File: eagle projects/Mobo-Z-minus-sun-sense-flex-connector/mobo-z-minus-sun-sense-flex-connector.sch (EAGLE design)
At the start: 2 parts

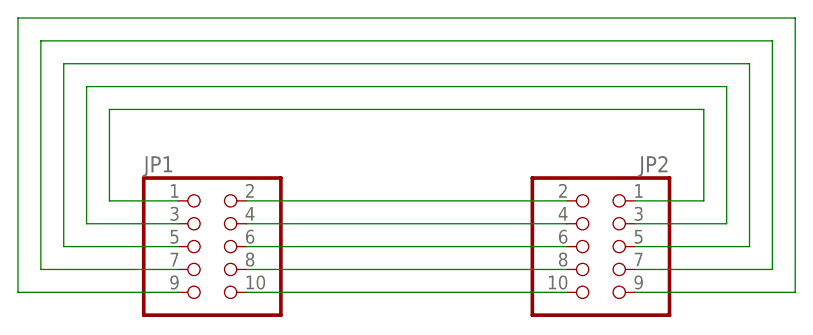
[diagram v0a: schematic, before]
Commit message: Created 5x2 SMD 2.54mm footprint and added it to board that needs it
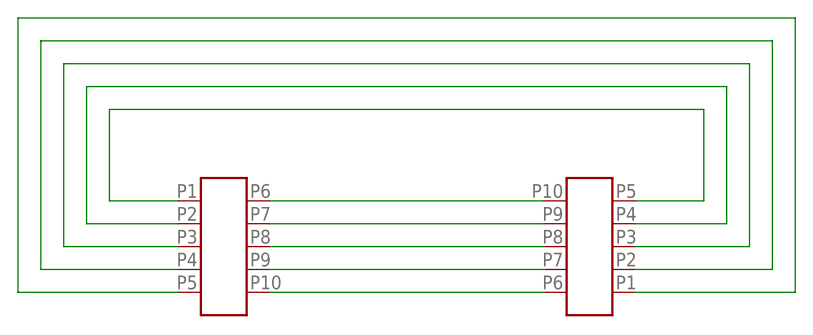
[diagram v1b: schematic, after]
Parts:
- removed JP1, JP2: (no value), pinhead:PINHD-2X5
- added X1, X2: 5X2_SMD_2.54MM_HEADER, SMD_headers:5X2_SMD_2.54MM_HEADER
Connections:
- net N$1: now also X1.P6, X2.P10; no longer JP1.2, JP2.2
- net N$10: now also X1.P5, X2.P1; no longer JP1.9, JP2.9
- net N$2: now also X1.P7, X2.P9; no longer JP1.4, JP2.4
- net N$3: now also X1.P8, X2.P8; no longer JP1.6, JP2.6
- net N$4: now also X1.P9, X2.P7; no longer JP1.8, JP2.8
- net N$5: now also X1.P10, X2.P6; no longer JP1.10, JP2.10
- net N$6: now also X1.P1, X2.P5; no longer JP1.1, JP2.1
- net N$7: now also X1.P2\, X2.P4; no longer JP1.3, JP2.3
- net N$8: now also X1.P3, X2.P3; no longer JP1.5, JP2.5
- net N$9: now also X1.P4, X2.P2\; no longer JP1.7, JP2.7
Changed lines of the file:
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@@
 </classes>
 <parts>
-<part name="JP1" library="pinhead" library_urn="urn:adsk.eagle:library:325" deviceset="PINHD-2X5" device="" package3d_urn="urn:adsk.eagle:package:22470/2"/>
-<part name="JP2" library="pinhead" library_urn="urn:adsk.eagle:library:325" deviceset="PINHD-2X5" device="" package3d_urn="urn:adsk.eagle:package:22470/2"/>
+<part name="X1" library="SMD_headers" deviceset="5X2_SMD_2.54MM_HEADER" device=""/>
+<part name="X2" library="SMD_headers" deviceset="5X2_SMD_2.54MM_HEADER" device=""/>
 </parts>
 <sheets>
@@
 </plain>
 <instances>
-<instance part="JP1" gate="A" x="30.48" y="53.34" smashed="yes">
-<attribute name="NAME" x="24.13" y="61.595" size="1.778" layer="95"/>
-<attribute name="VALUE" x="24.13" y="43.18" size="1.778" layer="96"/>
-</instance>
-<instance part="JP2" gate="A" x="76.2" y="53.34" smashed="yes" rot="MR0">
-<attribute name="NAME" x="82.55" y="61.595" size="1.778" layer="95" rot="MR0"/>
-<attribute name="VALUE" x="82.55" y="43.18" size="1.778" layer="96" rot="MR0"/>
-</instance>
+<instance part="X1" gate="G$1" x="33.02" y="53.34" smashed="yes"/>
+<instance part="X2" gate="G$1" x="73.66" y="53.34" smashed="yes" rot="R180"/>
 </instances>
 <busses>
 </busses>
 <nets>
+<net name="N$6" class="0">
+<segment>
+<wire x1="27.94" y1="58.42" x2="20.32" y2="58.42" width="0.1524" layer="91"/>
+<wire x1="20.32" y1="58.42" x2="20.32" y2="68.58" width="0.1524" layer="91"/>
+<wire x1="20.32" y1="68.58" x2="86.36" y2="68.58" width="0.1524" layer="91"/>
+<wire x1="86.36" y1="68.58" x2="86.36" y2="58.42" width="0.1524" layer="91"/>
+<wire x1="86.36" y1="58.42" x2="78.74" y2="58.42" width="0.1524" layer="91"/>
+<pinref part="X1" gate="G$1" pin="P1"/>
+<pinref part="X2" gate="G$1" pin="P5"/>
+</segment>
+</net>
+<net name="N$7" class="0">
+<segment>
+<wire x1="27.94" y1="55.88" x2="17.78" y2="55.88" width="0.1524" layer="91"/>
+<wire x1="17.78" y1="55.88" x2="17.78" y2="71.12" width="0.1524" layer="91"/>
+<wire x1="17.78" y1="71.12" x2="88.9" y2="71.12" width="0.1524" layer="91"/>
+<wire x1="88.9" y1="71.12" x2="88.9" y2="55.88" width="0.1524" layer="91"/>
+<wire x1="88.9" y1="55.88" x2="78.74" y2="55.88" width="0.1524" layer="91"/>
+<pinref part="X1" gate="G$1" pin="P2\"/>
+<pinref part="X2" gate="G$1" pin="P4"/>
+</segment>
+</net>
+<net name="N$8" class="0">
+<segment>
+<wire x1="78.74" y1="53.34" x2="91.44" y2="53.34" width="0.1524" layer="91"/>
+<wire x1="91.44" y1="53.34" x2="91.44" y2="73.66" width="0.1524" layer="91"/>
+<wire x1="91.44" y1="73.66" x2="15.24" y2="73.66" width="0.1524" layer="91"/>
+<wire x1="15.24" y1="73.66" x2="15.24" y2="53.34" width="0.1524" layer="91"/>
+<wire x1="15.24" y1="53.34" x2="27.94" y2="53.34" width="0.1524" layer="91"/>
+<pinref part="X1" gate="G$1" pin="P3"/>
+<pinref part="X2" gate="G$1" pin="P3"/>
+</segment>
+</net>
+<net name="N$9" class="0">
+<segment>
+<wire x1="27.94" y1="50.8" x2="12.7" y2="50.8" width="0.1524" layer="91"/>
+<wire x1="12.7" y1="50.8" x2="12.7" y2="76.2" width="0.1524" layer="91"/>
+<wire x1="12.7" y1="76.2" x2="93.98" y2="76.2" width="0.1524" layer="91"/>
+<wire x1="93.98" y1="76.2" x2="93.98" y2="50.8" width="0.1524" layer="91"/>
+<wire x1="93.98" y1="50.8" x2="78.74" y2="50.8" width="0.1524" layer="91"/>
+<pinref part="X1" gate="G$1" pin="P4"/>
+<pinref part="X2" gate="G$1" pin="P2\"/>
+</segment>
+</net>
+<net name="N$10" class="0">
+<segment>
+<wire x1="27.94" y1="48.26" x2="10.16" y2="48.26" width="0.1524" layer="91"/>
+<wire x1="10.16" y1="48.26" x2="10.16" y2="78.74" width="0.1524" layer="91"/>
+<wire x1="10.16" y1="78.74" x2="96.52" y2="78.74" width="0.1524" layer="91"/>
+<wire x1="96.52" y1="78.74" x2="96.52" y2="48.26" width="0.1524" layer="91"/>
+<wire x1="96.52" y1="48.26" x2="78.74" y2="48.26" width="0.1524" layer="91"/>
+<pinref part="X1" gate="G$1" pin="P5"/>
+<pinref part="X2" gate="G$1" pin="P1"/>
+</segment>
+</net>
 <net name="N$1" class="0">
 <segment>
-<pinref part="JP1" gate="A" pin="2"/>
-<pinref part="JP2" gate="A" pin="2"/>
-<wire x1="35.56" y1="58.42" x2="71.12" y2="58.42" width="0.1524" layer="91"/>
+<pinref part="X1" gate="G$1" pin="P6"/>
+<wire x1="38.1" y1="58.42" x2="68.58" y2="58.42" width="0.1524" layer="91"/>
+<pinref part="X2" gate="G$1" pin="P10"/>
 </segment>
 </net>
 <net name="N$2" class="0">
 <segment>
-<pinref part="JP1" gate="A" pin="4"/>
-<pinref part="JP2" gate="A" pin="4"/>
-<wire x1="35.56" y1="55.88" x2="71.12" y2="55.88" width="0.1524" layer="91"/>
+<pinref part="X1" gate="G$1" pin="P7"/>
+<wire x1="38.1" y1="55.88" x2="68.58" y2="55.88" width="0.1524" layer="91"/>
+<pinref part="X2" gate="G$1" pin="P9"/>
 </segment>
 </net>
 <net name="N$3" class="0">
 <segment>
-<pinref part="JP1" gate="A" pin="6"/>
-<pinref part="JP2" gate="A" pin="6"/>
-<wire x1="35.56" y1="53.34" x2="71.12" y2="53.34" width="0.1524" layer="91"/>
+<pinref part="X1" gate="G$1" pin="P8"/>
+<wire x1="38.1" y1="53.34" x2="68.58" y2="53.34" width="0.1524" layer="91"/>
+<pinref part="X2" gate="G$1" pin="P8"/>
 </segment>
 </net>
 <net name="N$4" class="0">
 <segment>
-<pinref part="JP1" gate="A" pin="8"/>
-<pinref part="JP2" gate="A" pin="8"/>
-<wire x1="35.56" y1="50.8" x2="71.12" y2="50.8" width="0.1524" layer="91"/>
+<pinref part="X1" gate="G$1" pin="P9"/>
+<wire x1="38.1" y1="50.8" x2="68.58" y2="50.8" width="0.1524" layer="91"/>
+<pinref part="X2" gate="G$1" pin="P7"/>
 </segment>
 </net>
 <net name="N$5" class="0">
 <segment>
-<pinref part="JP1" gate="A" pin="10"/>
-<pinref part="JP2" gate="A" pin="10"/>
-<wire x1="35.56" y1="48.26" x2="71.12" y2="48.26" width="0.1524" layer="91"/>
-</segment>
-</net>
-<net name="N$6" class="0">
-<segment>
-<pinref part="JP1" gate="A" pin="1"/>
-<wire x1="27.94" y1="58.42" x2="20.32" y2="58.42" width="0.1524" layer="91"/>
-<wire x1="20.32" y1="58.42" x2="20.32" y2="68.58" width="0.1524" layer="91"/>
-<wire x1="20.32" y1="68.58" x2="86.36" y2="68.58" width="0.1524" layer="91"/>
-<pinref part="JP2" gate="A" pin="1"/>
-<wire x1="86.36" y1="68.58" x2="86.36" y2="58.42" width="0.1524" layer="91"/>
-<wire x1="86.36" y1="58.42" x2="78.74" y2="58.42" width="0.1524" layer="91"/>
-</segment>
-</net>
-<net name="N$7" class="0">
-<segment>
-<pinref part="JP1" gate="A" pin="3"/>
-<wire x1="27.94" y1="55.88" x2="17.78" y2="55.88" width="0.1524" layer="91"/>
-<wire x1="17.78" y1="55.88" x2="17.78" y2="71.12" width="0.1524" layer="91"/>
-<wire x1="17.78" y1="71.12" x2="88.9" y2="71.12" width="0.1524" layer="91"/>
-<wire x1="88.9" y1="71.12" x2="88.9" y2="55.88" width="0.1524" layer="91"/>
-<pinref part="JP2" gate="A" pin="3"/>
-<wire x1="88.9" y1="55.88" x2="78.74" y2="55.88" width="0.1524" layer="91"/>
-</segment>
-</net>
-<net name="N$8" class="0">
-<segment>
-<pinref part="JP2" gate="A" pin="5"/>
-<wire x1="78.74" y1="53.34" x2="91.44" y2="53.34" width="0.1524" layer="91"/>
-<wire x1="91.44" y1="53.34" x2="91.44" y2="73.66" width="0.1524" layer="91"/>
-<wire x1="91.44" y1="73.66" x2="15.24" y2="73.66" width="0.1524" layer="91"/>
-<wire x1="15.24" y1="73.66" x2="15.24" y2="53.34" width="0.1524" layer="91"/>
-<pinref part="JP1" gate="A" pin="5"/>
-<wire x1="15.24" y1="53.34" x2="27.94" y2="53.34" width="0.1524" layer="91"/>
-</segment>
-</net>
-<net name="N$9" class="0">
-<segment>
-<pinref part="JP1" gate="A" pin="7"/>
-<wire x1="27.94" y1="50.8" x2="12.7" y2="50.8" width="0.1524" layer="91"/>
-<wire x1="12.7" y1="50.8" x2="12.7" y2="76.2" width="0.1524" layer="91"/>
-<wire x1="12.7" y1="76.2" x2="93.98" y2="76.2" width="0.1524" layer="91"/>
-<pinref part="JP2" gate="A" pin="7"/>
-<wire x1="93.98" y1="76.2" x2="93.98" y2="50.8" width="0.1524" layer="91"/>
-<wire x1="93.98" y1="50.8" x2="78.74" y2="50.8" width="0.1524" layer="91"/>
-</segment>
-</net>
-<net name="N$10" class="0">
-<segment>
-<pinref part="JP1" gate="A" pin="9"/>
-<wire x1="27.94" y1="48.26" x2="10.16" y2="48.26" width="0.1524" layer="91"/>
-<wire x1="10.16" y1="48.26" x2="10.16" y2="78.74" width="0.1524" layer="91"/>
-<wire x1="10.16" y1="78.74" x2="96.52" y2="78.74" width="0.1524" layer="91"/>
-<wire x1="96.52" y1="78.74" x2="96.52" y2="48.26" width="0.1524" layer="91"/>
-<pinref part="JP2" gate="A" pin="9"/>
-<wire x1="96.52" y1="48.26" x2="78.74" y2="48.26" width="0.1524" layer="91"/>
+<pinref part="X1" gate="G$1" pin="P10"/>
+<wire x1="38.1" y1="48.26" x2="68.58" y2="48.26" width="0.1524" layer="91"/>
+<pinref part="X2" gate="G$1" pin="P6"/>
 </segment>
 </net>
@@
 </schematic>
 </drawing>
-<compatibility>
-<note version="8.2" severity="warning">
-Since Version 8.2, EAGLE supports online libraries. The ids
-of those online libraries will not be understood (or retained)
-with this version.
-</note>
-<note version="8.3" severity="warning">
-Since Version 8.3, EAGLE supports URNs for individual library
-assets (packages, symbols, and devices). The URNs of those assets
-will not be understood (or retained) with this version.
-</note>
-<note version="8.3" severity="warning">
-Since Version 8.3, EAGLE supports the association of 3D packages
-with devices in libraries, schematics, and board files. Those 3D
-packages will not be understood (or retained) with this version.
-</note>
-</compatibility>
 </eagle>

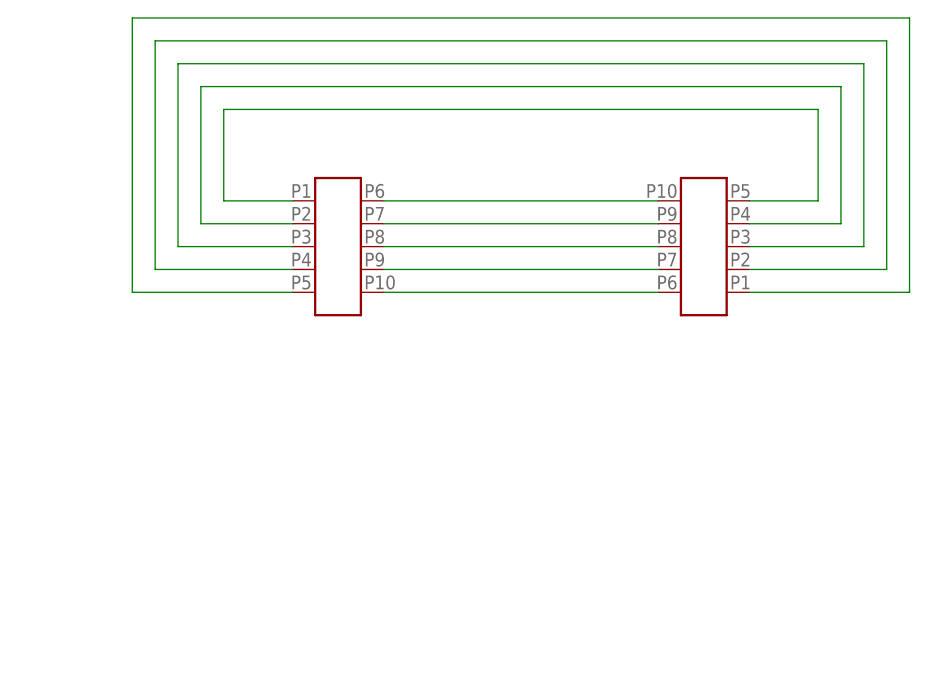
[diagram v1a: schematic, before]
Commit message: Fixed Connector Boards
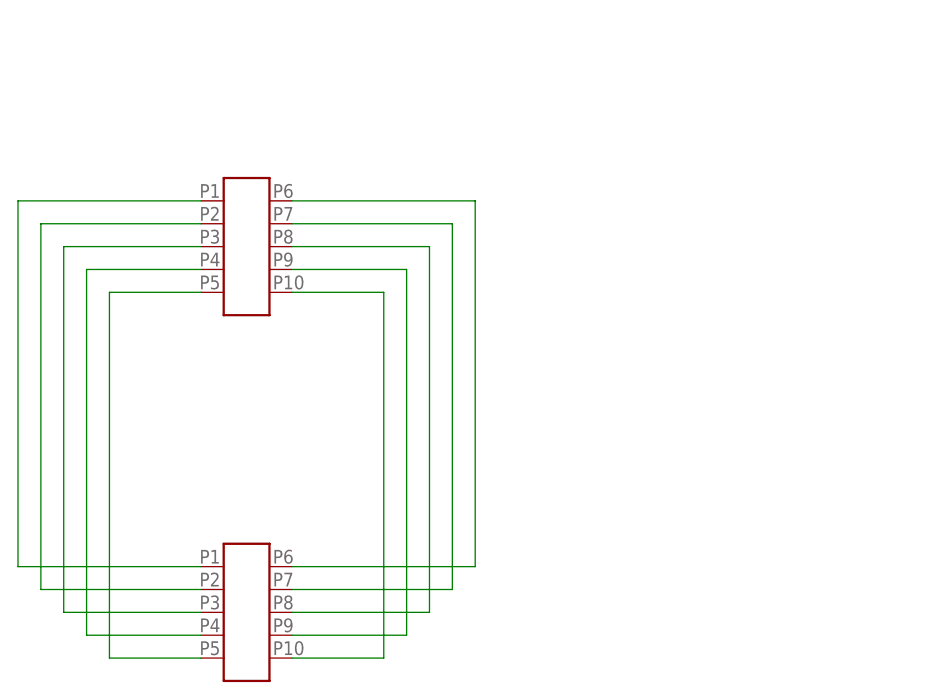
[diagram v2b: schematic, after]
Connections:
- net N$1: now also X2.P6; no longer X2.P10
- net N$10: now also X1.P1; no longer X1.P5
- net N$2: now also X2.P7; no longer X2.P9
- net N$4: now also X2.P9; no longer X2.P7
- net N$5: now also X2.P10; no longer X2.P6
- net N$6: now also X1.P5; no longer X1.P1
- net N$7: now also X1.P4; no longer X1.P2\
- net N$9: now also X1.P2\; no longer X1.P4
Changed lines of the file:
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@@
 </plain>
 <instances>
-<instance part="X1" gate="G$1" x="33.02" y="53.34" smashed="yes"/>
-<instance part="X2" gate="G$1" x="73.66" y="53.34" smashed="yes" rot="R180"/>
+<instance part="X1" gate="G$1" x="22.86" y="12.7" smashed="yes"/>
+<instance part="X2" gate="G$1" x="22.86" y="53.34" smashed="yes"/>
 </instances>
 <busses>
 </busses>
 <nets>
+<net name="N$1" class="0">
+<segment>
+<pinref part="X2" gate="G$1" pin="P6"/>
+<wire x1="27.94" y1="58.42" x2="48.26" y2="58.42" width="0.1524" layer="91"/>
+<pinref part="X1" gate="G$1" pin="P6"/>
+<wire x1="48.26" y1="58.42" x2="48.26" y2="17.78" width="0.1524" layer="91"/>
+<wire x1="48.26" y1="17.78" x2="27.94" y2="17.78" width="0.1524" layer="91"/>
+</segment>
+</net>
+<net name="N$2" class="0">
+<segment>
+<pinref part="X2" gate="G$1" pin="P7"/>
+<wire x1="27.94" y1="55.88" x2="45.72" y2="55.88" width="0.1524" layer="91"/>
+<wire x1="45.72" y1="55.88" x2="45.72" y2="15.24" width="0.1524" layer="91"/>
+<pinref part="X1" gate="G$1" pin="P7"/>
+<wire x1="45.72" y1="15.24" x2="27.94" y2="15.24" width="0.1524" layer="91"/>
+</segment>
+</net>
+<net name="N$3" class="0">
+<segment>
+<pinref part="X2" gate="G$1" pin="P8"/>
+<wire x1="27.94" y1="53.34" x2="43.18" y2="53.34" width="0.1524" layer="91"/>
+<wire x1="43.18" y1="53.34" x2="43.18" y2="12.7" width="0.1524" layer="91"/>
+<pinref part="X1" gate="G$1" pin="P8"/>
+<wire x1="43.18" y1="12.7" x2="27.94" y2="12.7" width="0.1524" layer="91"/>
+</segment>
+</net>
+<net name="N$4" class="0">
+<segment>
+<pinref part="X2" gate="G$1" pin="P9"/>
+<wire x1="27.94" y1="50.8" x2="40.64" y2="50.8" width="0.1524" layer="91"/>
+<wire x1="40.64" y1="50.8" x2="40.64" y2="10.16" width="0.1524" layer="91"/>
+<pinref part="X1" gate="G$1" pin="P9"/>
+<wire x1="40.64" y1="10.16" x2="27.94" y2="10.16" width="0.1524" layer="91"/>
+</segment>
+</net>
+<net name="N$5" class="0">
+<segment>
+<pinref part="X2" gate="G$1" pin="P10"/>
+<wire x1="27.94" y1="48.26" x2="38.1" y2="48.26" width="0.1524" layer="91"/>
+<pinref part="X1" gate="G$1" pin="P10"/>
+<wire x1="38.1" y1="48.26" x2="38.1" y2="7.62" width="0.1524" layer="91"/>
+<wire x1="38.1" y1="7.62" x2="27.94" y2="7.62" width="0.1524" layer="91"/>
+</segment>
+</net>
 <net name="N$6" class="0">
 <segment>
-<wire x1="27.94" y1="58.42" x2="20.32" y2="58.42" width="0.1524" layer="91"/>
-<wire x1="20.32" y1="58.42" x2="20.32" y2="68.58" width="0.1524" layer="91"/>
-<wire x1="20.32" y1="68.58" x2="86.36" y2="68.58" width="0.1524" layer="91"/>
-<wire x1="86.36" y1="68.58" x2="86.36" y2="58.42" width="0.1524" layer="91"/>
-<wire x1="86.36" y1="58.42" x2="78.74" y2="58.42" width="0.1524" layer="91"/>
-<pinref part="X1" gate="G$1" pin="P1"/>
 <pinref part="X2" gate="G$1" pin="P5"/>
+<wire x1="17.78" y1="48.26" x2="7.62" y2="48.26" width="0.1524" layer="91"/>
+<pinref part="X1" gate="G$1" pin="P5"/>
+<wire x1="7.62" y1="48.26" x2="7.62" y2="7.62" width="0.1524" layer="91"/>
+<wire x1="7.62" y1="7.62" x2="17.78" y2="7.62" width="0.1524" layer="91"/>
 </segment>
 </net>
 <net name="N$7" class="0">
 <segment>
-<wire x1="27.94" y1="55.88" x2="17.78" y2="55.88" width="0.1524" layer="91"/>
-<wire x1="17.78" y1="55.88" x2="17.78" y2="71.12" width="0.1524" layer="91"/>
-<wire x1="17.78" y1="71.12" x2="88.9" y2="71.12" width="0.1524" layer="91"/>
-<wire x1="88.9" y1="71.12" x2="88.9" y2="55.88" width="0.1524" layer="91"/>
-<wire x1="88.9" y1="55.88" x2="78.74" y2="55.88" width="0.1524" layer="91"/>
-<pinref part="X1" gate="G$1" pin="P2\"/>
+<pinref part="X1" gate="G$1" pin="P4"/>
+<wire x1="17.78" y1="10.16" x2="5.08" y2="10.16" width="0.1524" layer="91"/>
+<wire x1="5.08" y1="10.16" x2="5.08" y2="50.8" width="0.1524" layer="91"/>
 <pinref part="X2" gate="G$1" pin="P4"/>
+<wire x1="5.08" y1="50.8" x2="17.78" y2="50.8" width="0.1524" layer="91"/>
 </segment>
 </net>
 <net name="N$8" class="0">
 <segment>
-<wire x1="78.74" y1="53.34" x2="91.44" y2="53.34" width="0.1524" layer="91"/>
-<wire x1="91.44" y1="53.34" x2="91.44" y2="73.66" width="0.1524" layer="91"/>
-<wire x1="91.44" y1="73.66" x2="15.24" y2="73.66" width="0.1524" layer="91"/>
-<wire x1="15.24" y1="73.66" x2="15.24" y2="53.34" width="0.1524" layer="91"/>
-<wire x1="15.24" y1="53.34" x2="27.94" y2="53.34" width="0.1524" layer="91"/>
+<pinref part="X2" gate="G$1" pin="P3"/>
+<wire x1="17.78" y1="53.34" x2="2.54" y2="53.34" width="0.1524" layer="91"/>
+<wire x1="2.54" y1="53.34" x2="2.54" y2="12.7" width="0.1524" layer="91"/>
 <pinref part="X1" gate="G$1" pin="P3"/>
-<pinref part="X2" gate="G$1" pin="P3"/>
+<wire x1="2.54" y1="12.7" x2="17.78" y2="12.7" width="0.1524" layer="91"/>
 </segment>
 </net>
 <net name="N$9" class="0">
 <segment>
-<wire x1="27.94" y1="50.8" x2="12.7" y2="50.8" width="0.1524" layer="91"/>
-<wire x1="12.7" y1="50.8" x2="12.7" y2="76.2" width="0.1524" layer="91"/>
-<wire x1="12.7" y1="76.2" x2="93.98" y2="76.2" width="0.1524" layer="91"/>
-<wire x1="93.98" y1="76.2" x2="93.98" y2="50.8" width="0.1524" layer="91"/>
-<wire x1="93.98" y1="50.8" x2="78.74" y2="50.8" width="0.1524" layer="91"/>
-<pinref part="X1" gate="G$1" pin="P4"/>
+<pinref part="X1" gate="G$1" pin="P2\"/>
+<wire x1="17.78" y1="15.24" x2="0" y2="15.24" width="0.1524" layer="91"/>
+<wire x1="0" y1="15.24" x2="0" y2="55.88" width="0.1524" layer="91"/>
 <pinref part="X2" gate="G$1" pin="P2\"/>
+<wire x1="0" y1="55.88" x2="17.78" y2="55.88" width="0.1524" layer="91"/>
 </segment>
 </net>
 <net name="N$10" class="0">
 <segment>
-<wire x1="27.94" y1="48.26" x2="10.16" y2="48.26" width="0.1524" layer="91"/>
-<wire x1="10.16" y1="48.26" x2="10.16" y2="78.74" width="0.1524" layer="91"/>
-<wire x1="10.16" y1="78.74" x2="96.52" y2="78.74" width="0.1524" layer="91"/>
-<wire x1="96.52" y1="78.74" x2="96.52" y2="48.26" width="0.1524" layer="91"/>
-<wire x1="96.52" y1="48.26" x2="78.74" y2="48.26" width="0.1524" layer="91"/>
-<pinref part="X1" gate="G$1" pin="P5"/>
 <pinref part="X2" gate="G$1" pin="P1"/>
+<wire x1="17.78" y1="58.42" x2="-2.54" y2="58.42" width="0.1524" layer="91"/>
+<wire x1="-2.54" y1="58.42" x2="-2.54" y2="17.78" width="0.1524" layer="91"/>
+<pinref part="X1" gate="G$1" pin="P1"/>
+<wire x1="-2.54" y1="17.78" x2="17.78" y2="17.78" width="0.1524" layer="91"/>
 </segment>
 </net>
-<net name="N$1" class="0">
-<segment>
-<pinref part="X1" gate="G$1" pin="P6"/>
-<wire x1="38.1" y1="58.42" x2="68.58" y2="58.42" width="0.1524" layer="91"/>
-<pinref part="X2" gate="G$1" pin="P10"/>
-</segment>
-</net>
-<net name="N$2" class="0">
-<segment>
-<pinref part="X1" gate="G$1" pin="P7"/>
-<wire x1="38.1" y1="55.88" x2="68.58" y2="55.88" width="0.1524" layer="91"/>
-<pinref part="X2" gate="G$1" pin="P9"/>
-</segment>
-</net>
-<net name="N$3" class="0">
-<segment>
-<pinref part="X1" gate="G$1" pin="P8"/>
-<wire x1="38.1" y1="53.34" x2="68.58" y2="53.34" width="0.1524" layer="91"/>
-<pinref part="X2" gate="G$1" pin="P8"/>
-</segment>
-</net>
-<net name="N$4" class="0">
-<segment>
-<pinref part="X1" gate="G$1" pin="P9"/>
-<wire x1="38.1" y1="50.8" x2="68.58" y2="50.8" width="0.1524" layer="91"/>
-<pinref part="X2" gate="G$1" pin="P7"/>
-</segment>
-</net>
-<net name="N$5" class="0">
-<segment>
-<pinref part="X1" gate="G$1" pin="P10"/>
-<wire x1="38.1" y1="48.26" x2="68.58" y2="48.26" width="0.1524" layer="91"/>
-<pinref part="X2" gate="G$1" pin="P6"/>
-</segment>
-</net>
